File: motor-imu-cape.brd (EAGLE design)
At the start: 54.3 x 58.4 mm, 20 parts, among them IC1 40109, IC2 40109, IC3 24LC256P

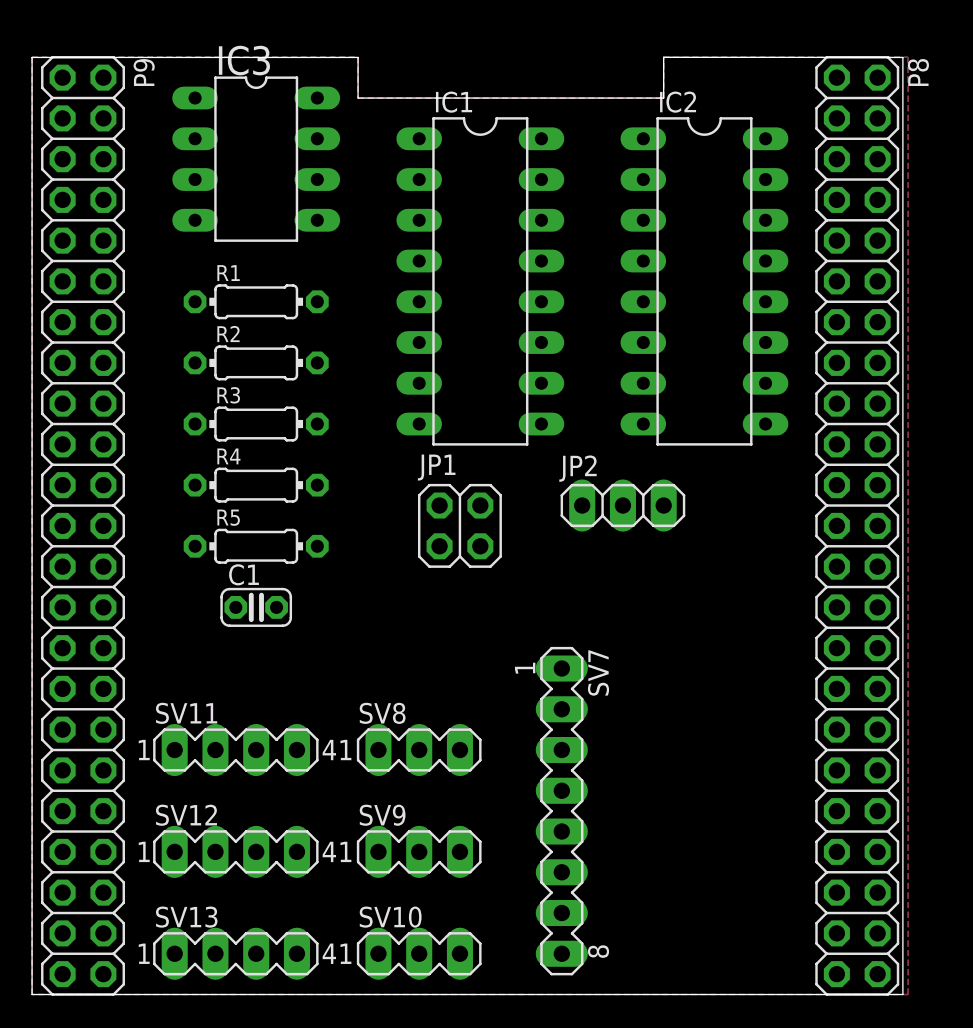
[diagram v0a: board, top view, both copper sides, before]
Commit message: Autoroute traces and get ready for logo
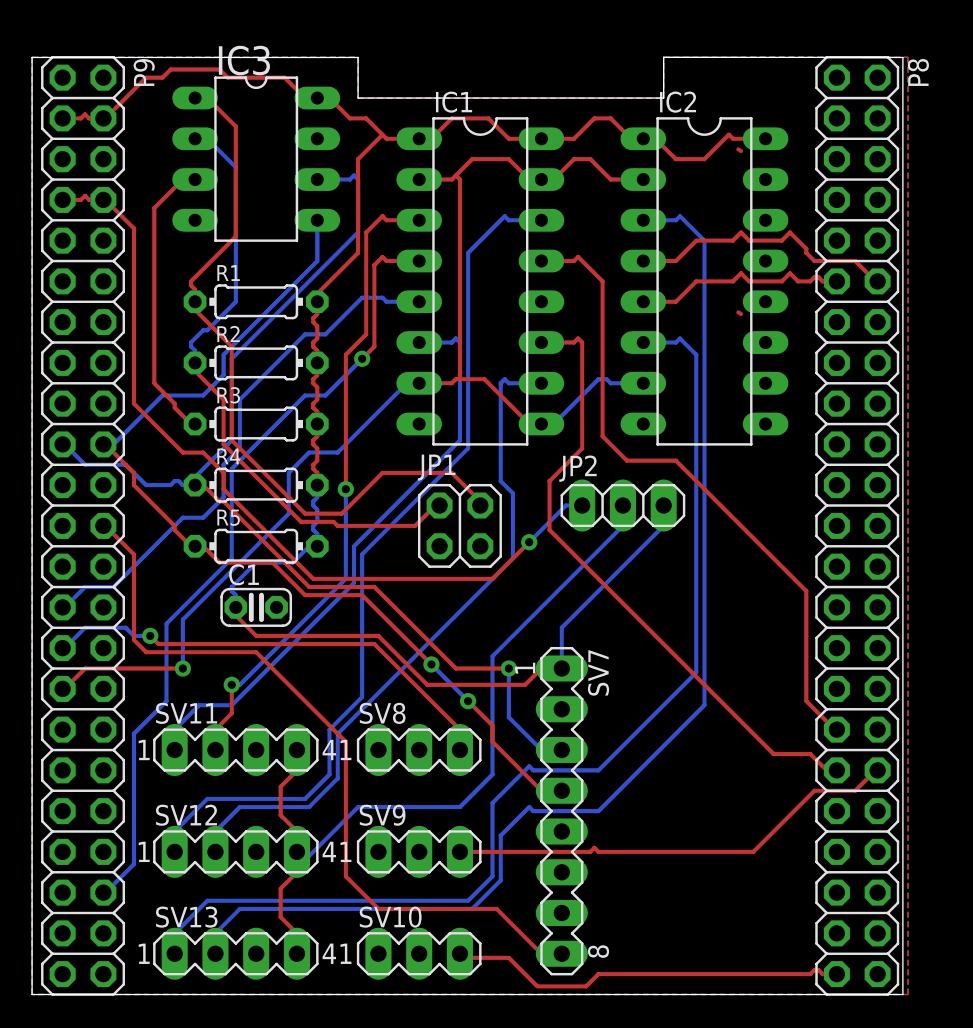
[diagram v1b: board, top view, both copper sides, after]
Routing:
- net +3V3: track 0.00 -> 123.1 mm
- net QEP_EN: track 0.00 -> 78.8 mm, vias 0 -> 1
- net QEP2A: track 0.00 -> 73.0 mm
- net I2C2_SCL: track 0.00 -> 67.2 mm, vias 0 -> 1
- net QEP2B: track 0.00 -> 67.0 mm
- net I2C2_SDA: track 0.00 -> 60.1 mm, vias 0 -> 2
- net QEP1B: track 0.00 -> 54.1 mm
- net +5V: track 0.00 -> 51.3 mm, vias 0 -> 1
- net EQEP0A: track 0.00 -> 50.0 mm, vias 0 -> 1
- net V_QEP: track 0.00 -> 48.9 mm
- net MPUINT: track 0.00 -> 47.7 mm
- net N$5: track 0.00 -> 44.5 mm
- net QEP1A: track 0.00 -> 42.5 mm
- net EQEP1B: track 0.00 -> 40.4 mm
- net QEP0A: track 0.00 -> 40.3 mm, vias 0 -> 2
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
